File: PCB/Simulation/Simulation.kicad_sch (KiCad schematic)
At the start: 14 parts

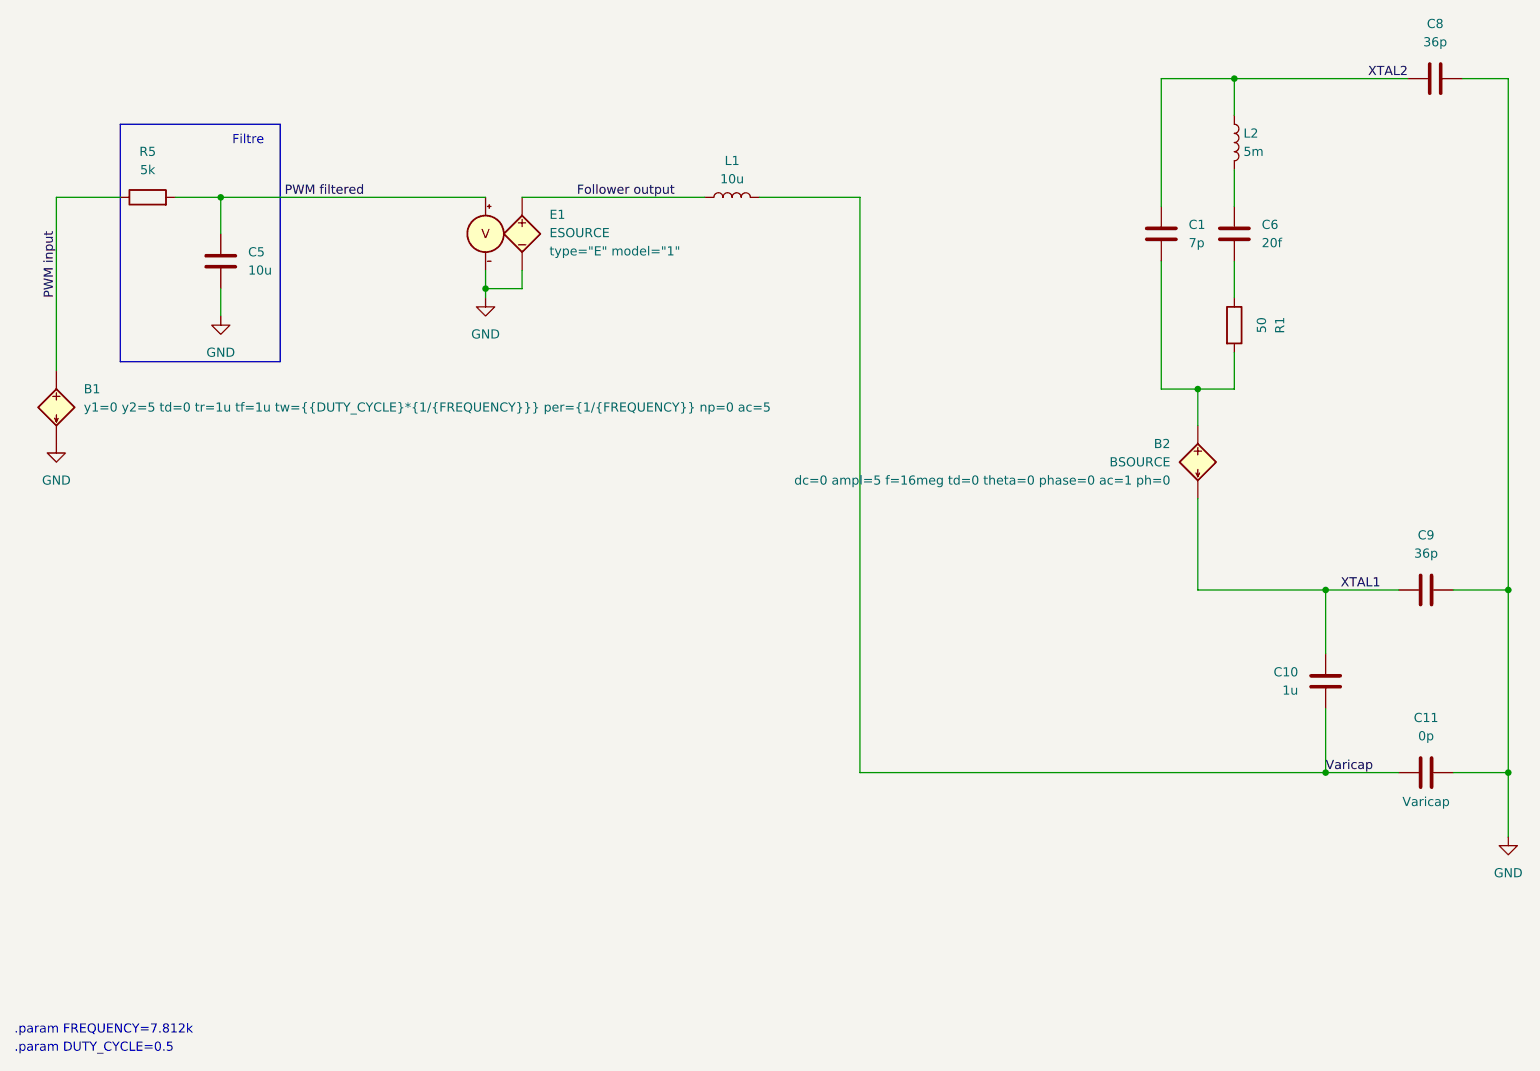
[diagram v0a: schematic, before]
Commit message: Réalisation de la simulation approximative de l'oscillateur
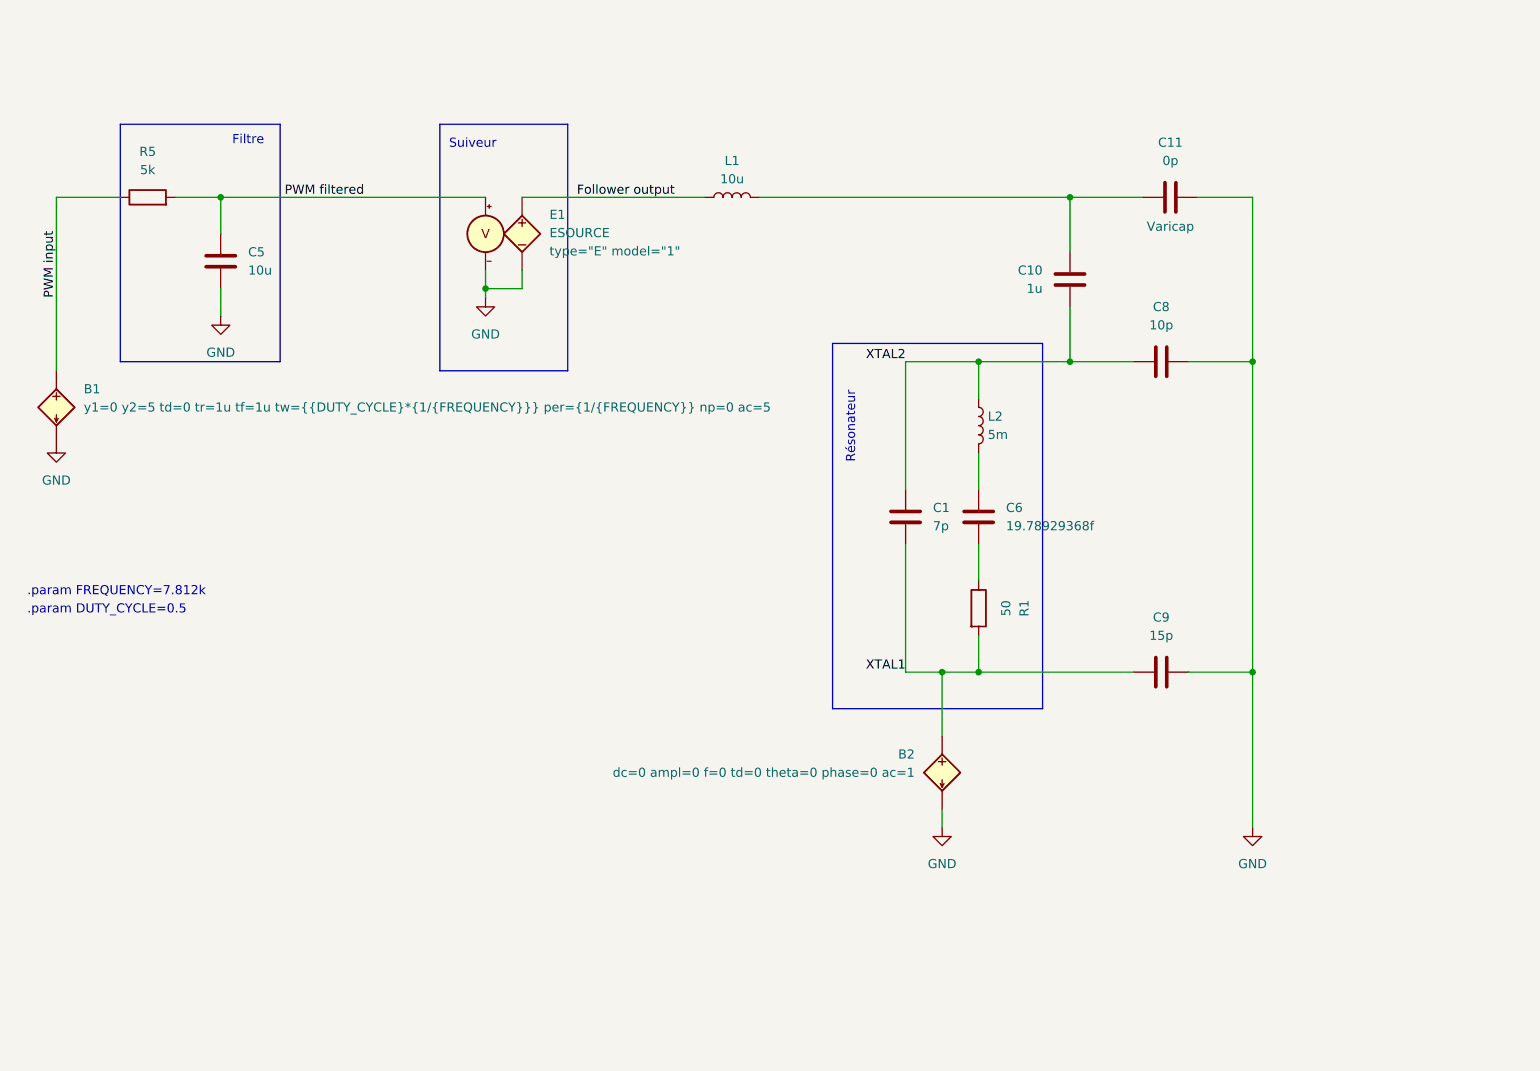
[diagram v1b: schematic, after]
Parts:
- B2: value BSOURCE -> ${SIM.PARAMS}
- C10: Prix/U 0,0982 € -> 0,0742 €
- C6: value 20f -> 19.78929368f
- C8: value 36p -> 10p
- C9: value 36p -> 15p; Prix/U 0,067 € -> 0,0742 €
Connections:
- net GND: now also B2.2 (N-), C8.2, C9.2; no longer C8.1, C9.1
- net XTAL1: now also B2.1 (N+), C1.2, C9.1, R1.2; no longer B2.2 (N-), C10.1, C9.2
- net XTAL2: now also C10.1, C8.1; no longer C8.2
- net Varicap: no longer names the net of C10.2, C11.2, L1.1
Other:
- note added: "Résonateur"
- note added: "Suiveur"
- moved on the sheet: B2, C1, C11, C6, C8, L2, R1

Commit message: Simulation
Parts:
- C5: value 10u -> 1u
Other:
- note added: ".param FREQUENCY=62k"
- note removed: ".param FREQUENCY=7.812k"
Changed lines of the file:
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@@
 		)
 	)
-	(text ".param FREQUENCY=7.812k"
+	(text ".param FREQUENCY=62k"
 		(exclude_from_sim no)
 		(at 25.146 103.124 0)
@@
 			)
 		)
-		(property "Value" "10u"
+		(property "Value" "1u"
 			(at 55.88 58.4199 0)
 			(effects
@@
 		(at 29.21 77.47 0)
 		(unit 1)
-		(exclude_from_sim yes)
-		(in_bom yes)
-		(on_board yes)
+		(exclude_from_sim no)
+		(in_bom yes)
+		(on_board yes)

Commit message: Changements des fichiers pour la simulation (je ne sais plus ce qu'on a fait)
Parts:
- C11: value 0p -> 2.52p
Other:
- note added: ".param FREQUENCY=10k"
- note removed: ".param FREQUENCY=62k"
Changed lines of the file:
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@@
 		)
 	)
-	(text ".param FREQUENCY=62k"
+	(text ".param FREQUENCY=10k"
 		(exclude_from_sim no)
 		(at 25.146 103.124 0)
@@
 			)
 		)
-		(property "Value" "0p"
+		(property "Value" "2.52p"
 			(at 184.15 43.18 90)
 			(effects
@@
 			(effects
 				(font
+					(size 1.27 1.27)
+				)
+				(hide yes)
+			)
+		)
+		(property "Sim.Device" "C"
+			(at 232.41 232.41 0)
+			(effects
+				(font
+					(size 1.27 1.27)
+				)
+				(hide yes)
+			)
+		)
+		(property "Sim.Pins" "1=- 2=+"
+			(at 232.41 232.41 0)
+			(effects
+				(font

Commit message: simulation AC
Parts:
- C11: value 2.52p -> 2p
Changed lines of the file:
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@@
 			)
 		)
-		(property "Value" "2.52p"
+		(property "Value" "2p"
 			(at 184.15 43.18 90)
 			(effects
